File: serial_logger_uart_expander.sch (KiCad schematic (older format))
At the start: 55 parts, among them J1 CN6, J2 CN8, J3 CN5, J4 CN9, J5 Screw_Terminal_01x10, J6 Screw_Terminal_01x10, U1 M74HC4851, U10 2N7002PS, U11 2N7002PS, U12 2N7002PS, U13 2N7002PS, U14 ESDA17-5SC6, U15 NRF24L01_Breakout, U2 M74HC4851, U3 ESDA17-5SC6, U4 ESDA17-5SC6, U5 ESDA17-5SC6, U6 2N7002PS, U7 2N7002PS, U8 2N7002PS, U9 2N7002PS

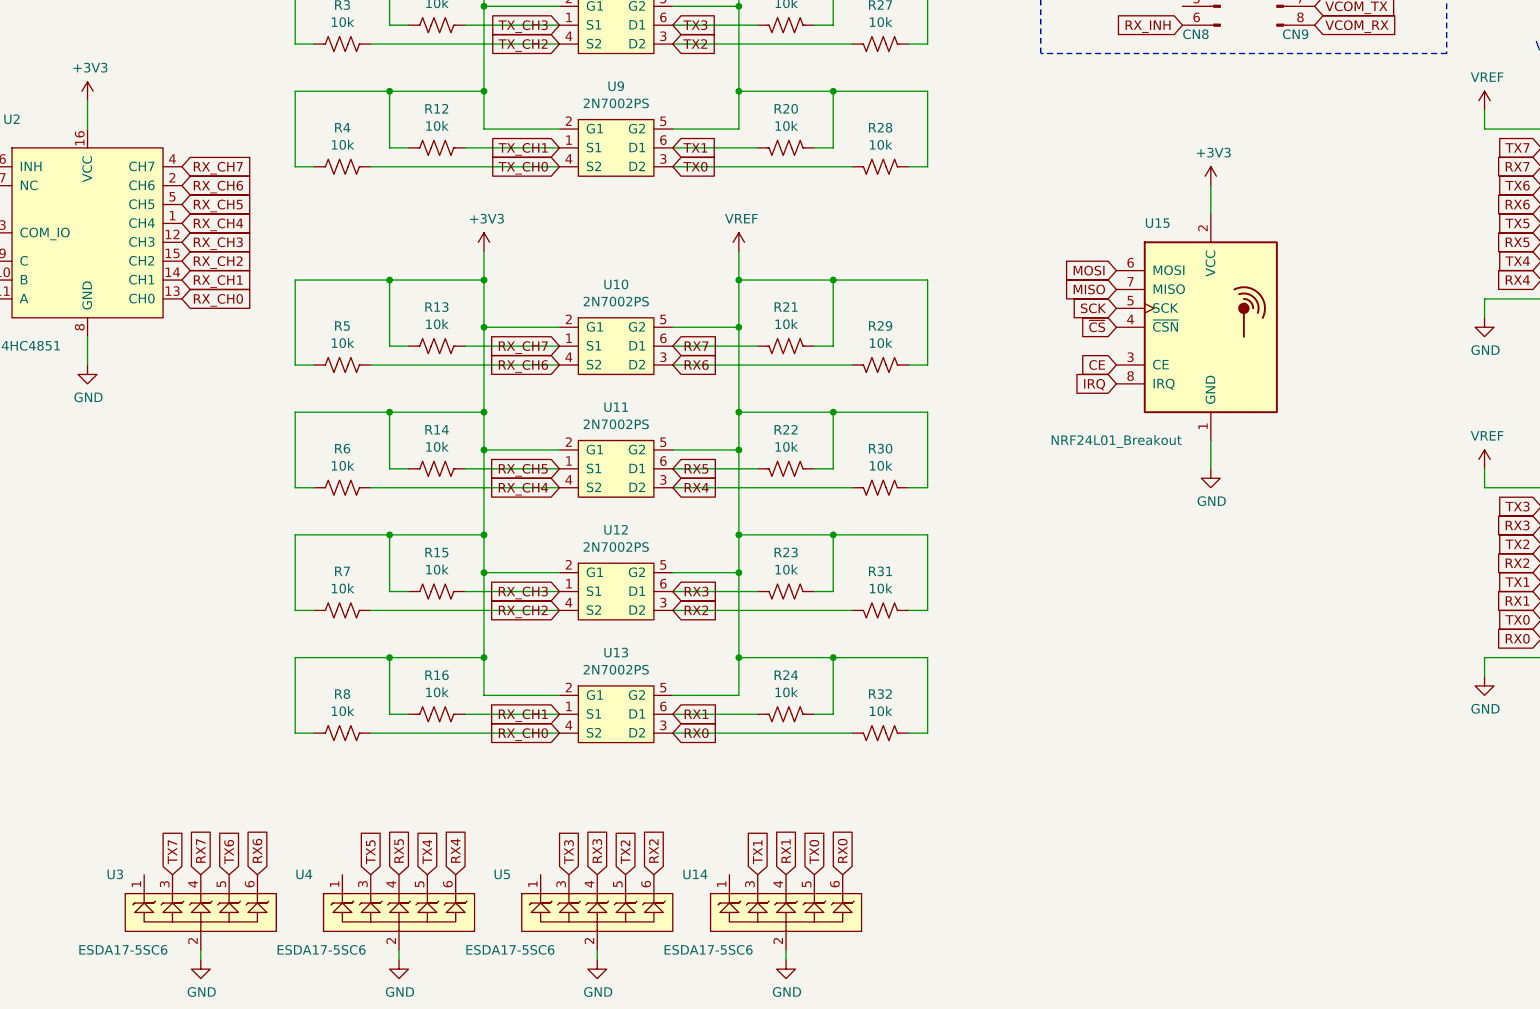
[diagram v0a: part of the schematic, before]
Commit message: rearranged components and traces
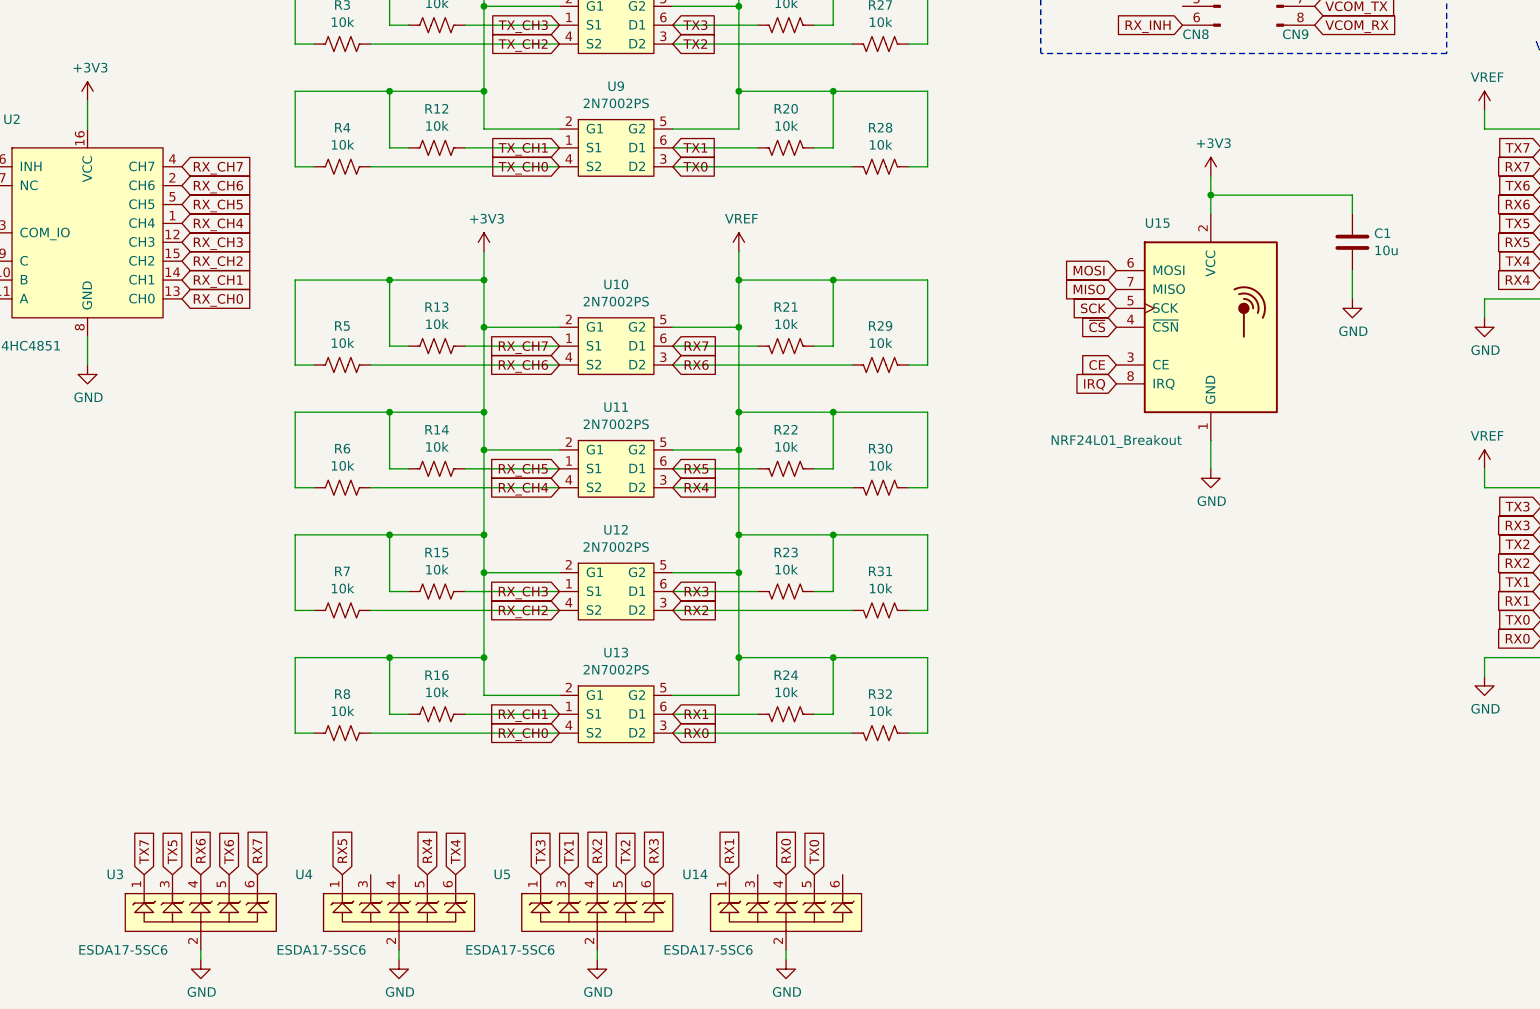
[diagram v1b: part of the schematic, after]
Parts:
- added C1: 10u, Capacitor_SMD:C_0805_2012Metric, symbol Device:C
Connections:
- net +3V3: now also C1.1
- net GND: now also C1.2
- net RX0: now also U14.4; no longer U14.6
- net RX1: now also U14.1; no longer U14.4
- net RX2: now also U5.4; no longer U5.6
- net RX3: now also U5.6; no longer U5.4
- net RX4: now also U4.5; no longer U4.6
- net RX5: now also U4.1; no longer U4.4
- net RX6: now also U3.4; no longer U3.6
- net RX7: now also U3.6; no longer U3.4
- net TX1: now also U5.3; no longer U14.3
- net TX3: now also U5.1; no longer U5.3
- net TX4: now also U4.6; no longer U4.5
- net TX5: now also U3.3; no longer U4.3
- net TX7: now also U3.1; no longer U3.3
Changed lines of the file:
@@
 Wire Wire Line
 	2100 7600 2100 7550
-Text GLabel 1950 7150 1    50   Input ~ 0
+Text GLabel 1800 7150 1    50   Input ~ 0
 TX7
-Text GLabel 2100 7150 1    50   Input ~ 0
+Text GLabel 2400 7150 1    50   Input ~ 0
 RX7
 Text GLabel 2250 7150 1    50   Input ~ 0
 TX6
-Text GLabel 2400 7150 1    50   Input ~ 0
+Text GLabel 2100 7150 1    50   Input ~ 0
 RX6
 $Comp
@@
 	1    0    0    -1
 $EndComp
+Text GLabel 3450 7150 1    50   Input ~ 0
+TX4
 Text GLabel 3300 7150 1    50   Input ~ 0
-TX4
-Text GLabel 3450 7150 1    50   Input ~ 0
 RX4
-Text GLabel 4050 7150 1    50   Input ~ 0
+Text GLabel 3900 7150 1    50   Input ~ 0
 TX3
-Text GLabel 4200 7150 1    50   Input ~ 0
+Text GLabel 4500 7150 1    50   Input ~ 0
 RX3
 $Comp
@@
 Wire Wire Line
 	4200 7600 4200 7550
-Text GLabel 3000 7150 1    50   Input ~ 0
+Text GLabel 1950 7150 1    50   Input ~ 0
 TX5
-Text GLabel 3150 7150 1    50   Input ~ 0
+Text GLabel 2850 7150 1    50   Input ~ 0
 RX5
 Text GLabel 4350 7150 1    50   Input ~ 0
 TX2
-Text GLabel 4500 7150 1    50   Input ~ 0
+Text GLabel 4200 7150 1    50   Input ~ 0
 RX2
 $Comp
@@
 	1    0    0    -1
 $EndComp
-Text GLabel 5050 7150 1    50   Input ~ 0
+Text GLabel 4050 7150 1    50   Input ~ 0
 TX1
-Text GLabel 5200 7150 1    50   Input ~ 0
+Text GLabel 4900 7150 1    50   Input ~ 0
 RX1
 Text GLabel 5350 7150 1    50   Input ~ 0
 TX0
-Text GLabel 5500 7150 1    50   Input ~ 0
+Text GLabel 5200 7150 1    50   Input ~ 0
 RX0
 $Comp
@@
 L power:+3V3 #PWR016
 U 1 1 6232743A
-P 7450 3500
-F 0 "#PWR016" H 7450 3350 50  0001 C CNN
-F 1 "+3V3" H 7465 3673 50  0000 C CNN
-F 2 "" H 7450 3500 50  0001 C CNN
-F 3 "" H 7450 3500 50  0001 C CNN
-	1    7450 3500
-	1    0    0    -1
-$EndComp
-Wire Wire Line
-	7450 3500 7450 3650
+P 7450 3450
+F 0 "#PWR016" H 7450 3300 50  0001 C CNN
+F 1 "+3V3" H 7465 3623 50  0000 C CNN
+F 2 "" H 7450 3450 50  0001 C CNN
+F 3 "" H 7450 3450 50  0001 C CNN
+	1    7450 3450
+	1    0    0    -1
+$EndComp
+Wire Wire Line
+	7450 3450 7450 3550
 Text GLabel 8000 2650 2    50   Input ~ 0
 VCOM_RX
@@
 	1    0    0    -1
 $EndComp
+$Comp
+L Device:C C1
+U 1 1 6136BA4A
+P 8200 3800
+F 0 "C1" H 8315 3846 50  0000 L CNN
+F 1 "10u" H 8315 3755 50  0000 L CNN
+F 2 "Capacitor_SMD:C_0805_2012Metric" H 8238 3650 50  0001 C CNN
+F 3 "~" H 8200 3800 50  0001 C CNN
+	1    8200 3800
+	1    0    0    -1
+$EndComp
+Wire Wire Line
+	8200 3650 8200 3550
+Wire Wire Line
+	8200 3550 7450 3550
+Connection ~ 7450 3550
+Wire Wire Line
+	7450 3550 7450 3650
+$Comp
+L power:GND #PWR025
+U 1 1 61379B82
+P 8200 4100
+F 0 "#PWR025" H 8200 3850 50  0001 C CNN
+F 1 "GND" H 8205 3927 50  0000 C CNN
+F 2 "" H 8200 4100 50  0001 C CNN
+F 3 "" H 8200 4100 50  0001 C CNN
+	1    8200 4100
+	1    0    0    -1
+$EndComp
+Wire Wire Line
+	8200 4100 8200 3950
 $EndSCHEMATC

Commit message: completed design, no gerbers or BOM.
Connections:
- net RX0: now also U14.6; no longer U14.4
- net RX1: now also U14.4; no longer U14.1
- net RX2: now also U5.6; no longer U5.4
- net RX3: now also U5.4; no longer U5.6
- net RX4: now also U4.6; no longer U4.5
- net RX5: now also U4.4; no longer U4.1
- net RX6: now also U3.6; no longer U3.4
- net RX7: now also U3.4; no longer U3.6
- net TX1: now also U14.3; no longer U5.3
- net TX3: now also U5.3; no longer U5.1
- net TX4: now also U4.5; no longer U4.6
- net TX5: now also U4.3; no longer U3.3
- net TX7: now also U3.3; no longer U3.1
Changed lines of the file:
@@
 Text GLabel 4000 1350 0    50   Input ~ 0
 TX_CH7
-Text GLabel 4000 1450 0    50   Input ~ 0
-TX_CH6
 Text GLabel 4000 2000 0    50   Input ~ 0
 TX_CH5
@@
 Text GLabel 4000 4450 0    50   Input ~ 0
 RX_CH6
-Text GLabel 4000 4350 0    50   Input ~ 0
-RX_CH7
 $Comp
 L Connector:Screw_Terminal_01x10 J5
@@
 Text GLabel 4600 1350 2    50   Input ~ 0
 TX7
-Text GLabel 4600 1450 2    50   Input ~ 0
-TX6
 Text GLabel 4600 2000 2    50   Input ~ 0
 TX5
@@
 Text GLabel 4600 3400 2    50   Input ~ 0
 TX0
-Text GLabel 4600 4350 2    50   Input ~ 0
-RX7
 Text GLabel 4600 4450 2    50   Input ~ 0
 RX6
@@
 Wire Wire Line
 	2100 7600 2100 7550
-Text GLabel 1800 7150 1    50   Input ~ 0
+Text GLabel 1950 7150 1    50   Input ~ 0
 TX7
-Text GLabel 2400 7150 1    50   Input ~ 0
+Text GLabel 2100 7150 1    50   Input ~ 0
 RX7
-Text GLabel 2250 7150 1    50   Input ~ 0
-TX6
-Text GLabel 2100 7150 1    50   Input ~ 0
-RX6
 $Comp
 L my_lib:ESDA17-5SC6 U4
@@
 	1    0    0    -1
 $EndComp
+Text GLabel 3300 7150 1    50   Input ~ 0
+TX4
 Text GLabel 3450 7150 1    50   Input ~ 0
-TX4
-Text GLabel 3300 7150 1    50   Input ~ 0
 RX4
-Text GLabel 3900 7150 1    50   Input ~ 0
+Text GLabel 4050 7150 1    50   Input ~ 0
 TX3
-Text GLabel 4500 7150 1    50   Input ~ 0
+Text GLabel 4200 7150 1    50   Input ~ 0
 RX3
 $Comp
@@
 Wire Wire Line
 	4200 7600 4200 7550
-Text GLabel 1950 7150 1    50   Input ~ 0
-TX5
-Text GLabel 2850 7150 1    50   Input ~ 0
+Text GLabel 3150 7150 1    50   Input ~ 0
 RX5
 Text GLabel 4350 7150 1    50   Input ~ 0
 TX2
-Text GLabel 4200 7150 1    50   Input ~ 0
+Text GLabel 4500 7150 1    50   Input ~ 0
 RX2
 $Comp
@@
 	1    0    0    -1
 $EndComp
-Text GLabel 4050 7150 1    50   Input ~ 0
-TX1
-Text GLabel 4900 7150 1    50   Input ~ 0
-RX1
-Text GLabel 5350 7150 1    50   Input ~ 0
-TX0
-Text GLabel 5200 7150 1    50   Input ~ 0
-RX0
 $Comp
 L Connector:Conn_01x06_Male J2
@@
 Wire Wire Line
 	8200 4100 8200 3950
+Text GLabel 4000 4350 0    50   Input ~ 0
+RX_CH7
+Text GLabel 4600 4350 2    50   Input ~ 0
+RX7
+Text GLabel 4000 1450 0    50   Input ~ 0
+TX_CH6
+Text GLabel 4600 1450 2    50   Input ~ 0
+TX6
+Text GLabel 2250 7150 1    50   Input ~ 0
+TX6
+Text GLabel 3000 7150 1    50   Input ~ 0
+TX5
+Text GLabel 2400 7150 1    50   Input ~ 0
+RX6
+Text GLabel 5050 7150 1    50   Input ~ 0
+TX1
+Text GLabel 5200 7150 1    50   Input ~ 0
+RX1
+Text GLabel 5350 7150 1    50   Input ~ 0
+TX0
+Text GLabel 5500 7150 1    50   Input ~ 0
+RX0
 $EndSCHEMATC

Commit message: v0.0 completed
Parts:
- C1: LCSC (none) -> C15850; LCSC Part # (none) -> C15850
- D1: LCSC (none) -> C72041; LCSC Part # (none) -> C72041
- R1, R10, R11, R12, R13, R14, R15, R16, R17, R18, R19, R2, R20, R21, R22, R23, R24, R25, R26, R27, R28, R29, R3, R30, R31, R32, R4, R5, R6, R7, R8, R9: LCSC (none) -> C25804; LCSC Part # (none) -> C25804
- R33: LCSC (none) -> C22843; LCSC Part # (none) -> C22843
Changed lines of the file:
@@
 F 2 "Resistor_SMD:R_0603_1608Metric" V 2890 1440 50  0001 C CNN
 F 3 "~" H 2850 1450 50  0001 C CNN
+F 4 "C25804" H 2850 1450 50  0001 C CNN "LCSC Part #"
+F 5 "C25804" H 2850 1450 50  0001 C CNN "LCSC"
 	1    2850 1450
 	0    1    1    0
@@
 F 2 "Resistor_SMD:R_0603_1608Metric" V 3390 1340 50  0001 C CNN
 F 3 "~" H 3350 1350 50  0001 C CNN
+F 4 "C25804" H 3350 1350 50  0001 C CNN "LCSC Part #"
+F 5 "C25804" H 3350 1350 50  0001 C CNN "LCSC"
 	1    3350 1350
 	0    1    1    0
@@
 F 2 "Resistor_SMD:R_0603_1608Metric" V 5240 1340 50  0001 C CNN
 F 3 "~" H 5200 1350 50  0001 C CNN
+F 4 "C25804" H 5200 1350 50  0001 C CNN "LCSC Part #"
+F 5 "C25804" H 5200 1350 50  0001 C CNN "LCSC"
 	1    5200 1350
 	0    1    -1   0
@@
 F 2 "Resistor_SMD:R_0603_1608Metric" V 2890 2090 50  0001 C CNN
 F 3 "~" H 2850 2100 50  0001 C CNN
+F 4 "C25804" H 2850 2100 50  0001 C CNN "LCSC Part #"
+F 5 "C25804" H 2850 2100 50  0001 C CNN "LCSC"
 	1    2850 2100
 	0    1    1    0
@@
 F 2 "Resistor_SMD:R_0603_1608Metric" V 3390 1990 50  0001 C CNN
 F 3 "~" H 3350 2000 50  0001 C CNN
+F 4 "C25804" H 3350 2000 50  0001 C CNN "LCSC Part #"
+F 5 "C25804" H 3350 2000 50  0001 C CNN "LCSC"
 	1    3350 2000
 	0    1    1    0
@@
 F 2 "Resistor_SMD:R_0603_1608Metric" V 5240 1990 50  0001 C CNN
 F 3 "~" H 5200 2000 50  0001 C CNN
+F 4 "C25804" H 5200 2000 50  0001 C CNN "LCSC Part #"
+F 5 "C25804" H 5200 2000 50  0001 C CNN "LCSC"
 	1    5200 2000
 	0    1    -1   0
@@
 F 2 "Resistor_SMD:R_0603_1608Metric" V 5740 2090 50  0001 C CNN
 F 3 "~" H 5700 2100 50  0001 C CNN
+F 4 "C25804" H 5700 2100 50  0001 C CNN "LCSC Part #"
+F 5 "C25804" H 5700 2100 50  0001 C CNN "LCSC"
 	1    5700 2100
 	0    1    -1   0
@@
 F 2 "Resistor_SMD:R_0603_1608Metric" V 2890 2740 50  0001 C CNN
 F 3 "~" H 2850 2750 50  0001 C CNN
+F 4 "C25804" H 2850 2750 50  0001 C CNN "LCSC Part #"
+F 5 "C25804" H 2850 2750 50  0001 C CNN "LCSC"
 	1    2850 2750
 	0    1    1    0
@@
 F 2 "Resistor_SMD:R_0603_1608Metric" V 3390 2640 50  0001 C CNN
 F 3 "~" H 3350 2650 50  0001 C CNN
+F 4 "C25804" H 3350 2650 50  0001 C CNN "LCSC Part #"
+F 5 "C25804" H 3350 2650 50  0001 C CNN "LCSC"
 	1    3350 2650
 	0    1    1    0
@@
 F 2 "Resistor_SMD:R_0603_1608Metric" V 5240 2640 50  0001 C CNN
 F 3 "~" H 5200 2650 50  0001 C CNN
+F 4 "C25804" H 5200 2650 50  0001 C CNN "LCSC Part #"
+F 5 "C25804" H 5200 2650 50  0001 C CNN "LCSC"
 	1    5200 2650
 	0    1    -1   0
@@
 F 2 "Resistor_SMD:R_0603_1608Metric" V 5740 2740 50  0001 C CNN
 F 3 "~" H 5700 2750 50  0001 C CNN
+F 4 "C25804" H 5700 2750 50  0001 C CNN "LCSC Part #"
+F 5 "C25804" H 5700 2750 50  0001 C CNN "LCSC"
 	1    5700 2750
 	0    1    -1   0
@@
 F 2 "Resistor_SMD:R_0603_1608Metric" V 2890 3390 50  0001 C CNN
 F 3 "~" H 2850 3400 50  0001 C CNN
+F 4 "C25804" H 2850 3400 50  0001 C CNN "LCSC Part #"
+F 5 "C25804" H 2850 3400 50  0001 C CNN "LCSC"
 	1    2850 3400
 	0    1    1    0
@@
 F 2 "Resistor_SMD:R_0603_1608Metric" V 3390 3290 50  0001 C CNN
 F 3 "~" H 3350 3300 50  0001 C CNN
+F 4 "C25804" H 3350 3300 50  0001 C CNN "LCSC Part #"
+F 5 "C25804" H 3350 3300 50  0001 C CNN "LCSC"
 	1    3350 3300
 	0    1    1    0
@@
 F 2 "Resistor_SMD:R_0603_1608Metric" V 5240 3290 50  0001 C CNN
 F 3 "~" H 5200 3300 50  0001 C CNN
+F 4 "C25804" H 5200 3300 50  0001 C CNN "LCSC Part #"
+F 5 "C25804" H 5200 3300 50  0001 C CNN "LCSC"
 	1    5200 3300
 	0    1    -1   0
@@
 F 2 "Resistor_SMD:R_0603_1608Metric" V 5740 3390 50  0001 C CNN
 F 3 "~" H 5700 3400 50  0001 C CNN
+F 4 "C25804" H 5700 3400 50  0001 C CNN "LCSC Part #"
+F 5 "C25804" H 5700 3400 50  0001 C CNN "LCSC"
 	1    5700 3400
 	0    1    -1   0
@@
 F 2 "Resistor_SMD:R_0603_1608Metric" V 2890 4440 50  0001 C CNN
 F 3 "~" H 2850 4450 50  0001 C CNN
+F 4 "C25804" H 2850 4450 50  0001 C CNN "LCSC Part #"
+F 5 "C25804" H 2850 4450 50  0001 C CNN "LCSC"
 	1    2850 4450
 	0    1    1    0
@@
 F 2 "Resistor_SMD:R_0603_1608Metric" V 3390 4340 50  0001 C CNN
 F 3 "~" H 3350 4350 50  0001 C CNN
+F 4 "C25804" H 3350 4350 50  0001 C CNN "LCSC Part #"
+F 5 "C25804" H 3350 4350 50  0001 C CNN "LCSC"
 	1    3350 4350
 	0    1    1    0
@@
 F 2 "Resistor_SMD:R_0603_1608Metric" V 5240 4340 50  0001 C CNN
 F 3 "~" H 5200 4350 50  0001 C CNN
+F 4 "C25804" H 5200 4350 50  0001 C CNN "LCSC Part #"
+F 5 "C25804" H 5200 4350 50  0001 C CNN "LCSC"
 	1    5200 4350
 	0    1    -1   0
@@
 F 2 "Resistor_SMD:R_0603_1608Metric" V 5740 4440 50  0001 C CNN
 F 3 "~" H 5700 4450 50  0001 C CNN
+F 4 "C25804" H 5700 4450 50  0001 C CNN "LCSC Part #"
+F 5 "C25804" H 5700 4450 50  0001 C CNN "LCSC"
 	1    5700 4450
 	0    1    -1   0
@@
 F 2 "Resistor_SMD:R_0603_1608Metric" V 2890 5090 50  0001 C CNN
 F 3 "~" H 2850 5100 50  0001 C CNN
+F 4 "C25804" H 2850 5100 50  0001 C CNN "LCSC Part #"
+F 5 "C25804" H 2850 5100 50  0001 C CNN "LCSC"
 	1    2850 5100
 	0    1    1    0
@@
 F 2 "Resistor_SMD:R_0603_1608Metric" V 3390 4990 50  0001 C CNN
 F 3 "~" H 3350 5000 50  0001 C CNN
+F 4 "C25804" H 3350 5000 50  0001 C CNN "LCSC Part #"
+F 5 "C25804" H 3350 5000 50  0001 C CNN "LCSC"
 	1    3350 5000
 	0    1    1    0
@@
 F 2 "Resistor_SMD:R_0603_1608Metric" V 5240 4990 50  0001 C CNN
 F 3 "~" H 5200 5000 50  0001 C CNN
+F 4 "C25804" H 5200 5000 50  0001 C CNN "LCSC Part #"
+F 5 "C25804" H 5200 5000 50  0001 C CNN "LCSC"
 	1    5200 5000
 	0    1    -1   0
@@
 F 2 "Resistor_SMD:R_0603_1608Metric" V 5740 5090 50  0001 C CNN
 F 3 "~" H 5700 5100 50  0001 C CNN
+F 4 "C25804" H 5700 5100 50  0001 C CNN "LCSC Part #"
+F 5 "C25804" H 5700 5100 50  0001 C CNN "LCSC"
 	1    5700 5100
 	0    1    -1   0
@@
 F 2 "Resistor_SMD:R_0603_1608Metric" V 2890 5740 50  0001 C CNN
 F 3 "~" H 2850 5750 50  0001 C CNN
+F 4 "C25804" H 2850 5750 50  0001 C CNN "LCSC Part #"
+F 5 "C25804" H 2850 5750 50  0001 C CNN "LCSC"
 	1    2850 5750
 	0    1    1    0
@@
 F 2 "Resistor_SMD:R_0603_1608Metric" V 3390 5640 50  0001 C CNN
 F 3 "~" H 3350 5650 50  0001 C CNN
+F 4 "C25804" H 3350 5650 50  0001 C CNN "LCSC Part #"
+F 5 "C25804" H 3350 5650 50  0001 C CNN "LCSC"
 	1    3350 5650
 	0    1    1    0
@@
 F 2 "Resistor_SMD:R_0603_1608Metric" V 5240 5640 50  0001 C CNN
 F 3 "~" H 5200 5650 50  0001 C CNN
+F 4 "C25804" H 5200 5650 50  0001 C CNN "LCSC Part #"
+F 5 "C25804" H 5200 5650 50  0001 C CNN "LCSC"
 	1    5200 5650
 	0    1    -1   0
@@
 F 2 "Resistor_SMD:R_0603_1608Metric" V 5740 5740 50  0001 C CNN
 F 3 "~" H 5700 5750 50  0001 C CNN
+F 4 "C25804" H 5700 5750 50  0001 C CNN "LCSC Part #"
+F 5 "C25804" H 5700 5750 50  0001 C CNN "LCSC"
 	1    5700 5750
 	0    1    -1   0
@@
 F 2 "Resistor_SMD:R_0603_1608Metric" V 2890 6390 50  0001 C CNN
 F 3 "~" H 2850 6400 50  0001 C CNN
+F 4 "C25804" H 2850 6400 50  0001 C CNN "LCSC Part #"
+F 5 "C25804" H 2850 6400 50  0001 C CNN "LCSC"
 	1    2850 6400
 	0    1    1    0
@@
 F 2 "Resistor_SMD:R_0603_1608Metric" V 3390 6290 50  0001 C CNN
 F 3 "~" H 3350 6300 50  0001 C CNN
+F 4 "C25804" H 3350 6300 50  0001 C CNN "LCSC Part #"
+F 5 "C25804" H 3350 6300 50  0001 C CNN "LCSC"
 	1    3350 6300
 	0    1    1    0
@@
 F 2 "Resistor_SMD:R_0603_1608Metric" V 5240 6290 50  0001 C CNN
 F 3 "~" H 5200 6300 50  0001 C CNN
+F 4 "C25804" H 5200 6300 50  0001 C CNN "LCSC Part #"
+F 5 "C25804" H 5200 6300 50  0001 C CNN "LCSC"
 	1    5200 6300
 	0    1    -1   0
@@
 F 2 "Resistor_SMD:R_0603_1608Metric" V 5740 6390 50  0001 C CNN
 F 3 "~" H 5700 6400 50  0001 C CNN
+F 4 "C25804" H 5700 6400 50  0001 C CNN "LCSC Part #"
+F 5 "C25804" H 5700 6400 50  0001 C CNN "LCSC"
 	1    5700 6400
 	0    1    -1   0
@@
 F 2 "Resistor_SMD:R_0603_1608Metric" V 5740 1440 50  0001 C CNN
 F 3 "~" H 5700 1450 50  0001 C CNN
+F 4 "C25804" H 5700 1450 50  0001 C CNN "LCSC Part #"
+F 5 "C25804" H 5700 1450 50  0001 C CNN "LCSC"
 	1    5700 1450
 	0    1    -1   0
@@
 F 2 "Resistor_SMD:R_0603_1608Metric" V 9990 1590 50  0001 C CNN
 F 3 "~" H 9950 1600 50  0001 C CNN
+F 4 "C22843" H 9950 1600 50  0001 C CNN "LCSC Part #"
+F 5 "C22843" H 9950 1600 50  0001 C CNN "LCSC"
 	1    9950 1600
 	1    0    0    1
@@
 F 2 "LED_SMD:LED_0603_1608Metric_Castellated" H 9950 1200 50  0001 C CNN
 F 3 "~" H 9950 1200 50  0001 C CNN
+F 4 "C72041" H 9950 1200 50  0001 C CNN "LCSC Part #"
+F 5 "C72041" H 9950 1200 50  0001 C CNN "LCSC"
 	1    9950 1200
 	0    -1   -1   0
@@
 F 2 "Capacitor_SMD:C_0805_2012Metric" H 8238 3650 50  0001 C CNN
 F 3 "~" H 8200 3800 50  0001 C CNN
+F 4 "C15850" H 8200 3800 50  0001 C CNN "LCSC Part #"
+F 5 "C15850" H 8200 3800 50  0001 C CNN "LCSC"
 	1    8200 3800
 	1    0    0    -1
